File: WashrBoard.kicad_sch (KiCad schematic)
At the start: 37 parts, among them J1 TestPoint 5V, J10 ProgPoint GND, J2 USB_C_Receptacle_USB2.0_16P, J3 TestPoint GND, J4 TestPoint 3.3V, J5 JST XH, J6 ProgPoint 5V, J7 ProgPoint P9 GND, J8 ProgPointPoint D_P, J9 ProgPoint D_N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

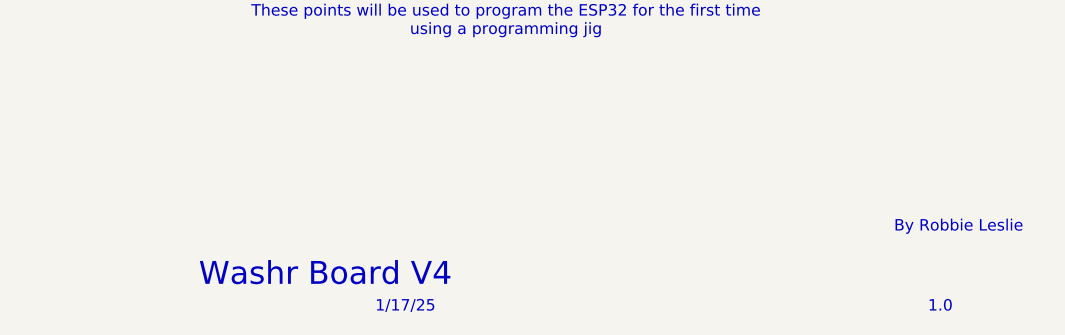
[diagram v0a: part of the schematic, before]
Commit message: Updated version, and moved old designs to archive repo
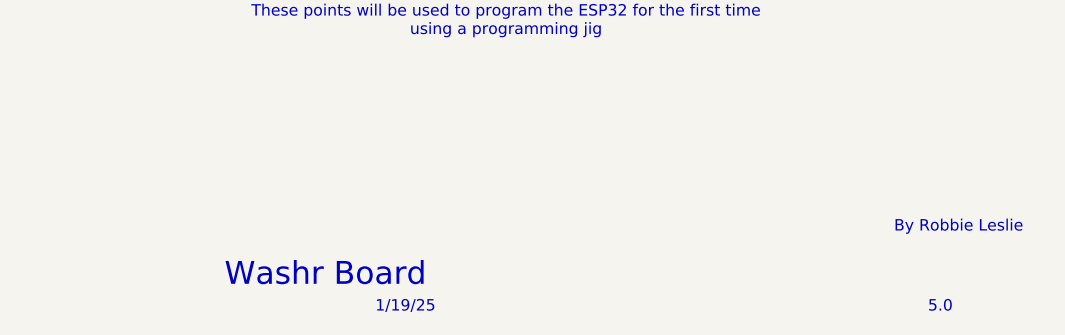
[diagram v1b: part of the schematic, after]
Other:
- note added: "1/19/25"
- note added: "5.0"
- note added: "Washr Board"
- note removed: "1.0"
- note removed: "1/17/25"
- note removed: "Washr Board V4"
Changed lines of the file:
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@@
 		)
 	)
-	(text "Washr Board V4"
+	(text "Washr Board"
 		(exclude_from_sim no)
 		(at 201.93 189.992 0)
@@
 		)
 	)
-	(text "1/17/25"
+	(text "1/19/25"
 		(exclude_from_sim no)
 		(at 210.82 193.548 0)
@@
 		)
 	)
-	(text "1.0"
+	(text "5.0"
 		(exclude_from_sim no)
 		(at 270.256 193.548 0)
@@
 	(label "SDA"
 		(at 54.61 92.71 0)
-		(fields_autoplaced yes)
 		(effects
 			(font
@@
 	(label "D_P"
 		(at 223.52 147.32 0)
-		(fields_autoplaced yes)
 		(effects
 			(font
@@
 	(label "D_P"
 		(at 63.5 151.13 0)
-		(fields_autoplaced yes)
 		(effects
 			(font
@@
 	(label "ProgGND"
 		(at 207.01 109.22 0)
-		(fields_autoplaced yes)
 		(effects
 			(font
@@
 	(label "D_P"
 		(at 92.71 34.29 0)
-		(fields_autoplaced yes)
 		(effects
 			(font
@@
 	(label "D_N"
 		(at 63.5 146.05 0)
-		(fields_autoplaced yes)
 		(effects
 			(font
@@
 	(label "ProgGND"
 		(at 223.52 135.89 0)
-		(fields_autoplaced yes)
 		(effects
 			(font
@@
 	(label "D-"
 		(at 213.36 81.28 0)
-		(fields_autoplaced yes)
 		(effects
 			(font
@@
 	(label "D+"
 		(at 213.36 83.82 0)
-		(fields_autoplaced yes)
 		(effects
 			(font
@@
 	(label "D_N"
 		(at 223.52 157.48 0)
-		(fields_autoplaced yes)
 		(effects
 			(font
@@
 	(label "D-"
 		(at 110.49 31.75 0)
-		(fields_autoplaced yes)
 		(effects
 			(font
@@
 	(label "SCL"
 		(at 54.61 90.17 0)
-		(fields_autoplaced yes)
 		(effects
 			(font
@@
 	(label "D_N"
 		(at 92.71 31.75 0)
-		(fields_autoplaced yes)
 		(effects
 			(font
@@
 	(label "SCL"
 		(at 177.8 66.04 0)
-		(fields_autoplaced yes)
 		(effects
 			(font
@@
 	(label "D+"
 		(at 110.49 34.29 0)
-		(fields_autoplaced yes)
 		(effects
 			(font
@@
 	(label "SDA"
 		(at 177.8 63.5 0)
-		(fields_autoplaced yes)
-		(effects
-			(font
+		(effects
+			(font

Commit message: Updated silkscreen
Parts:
- J1: TestValue (none) -> 5V
- J10: ProgPoint (none) -> PGND
- J3: TestValue (none) -> GND
- J4: TestValue (none) -> 3.3V
- J6: ProgPoint (none) -> 5V
- J7: ProgPoint (none) -> GND
- J8: ProgPoint (none) -> D_P
- J9: ProgPoint (none) -> D_N
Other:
- moved on the sheet: J1, J3, J4
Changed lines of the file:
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@@
 	(symbol
 		(lib_id "power:VBUS")
-		(at 26.67 60.96 90)
+		(at 129.54 157.48 270)
+		(mirror x)
 		(unit 1)
 		(exclude_from_sim no)
@@
 		(fields_autoplaced yes)
 		(property "Reference" "#PWR01"
-			(at 30.48 60.96 0)
+			(at 125.73 157.48 0)
 			(effects
 				(font
@@
 		)
 		(property "Value" "VBUS"
-			(at 22.86 60.9599 90)
+			(at 133.35 157.4799 90)
 			(effects
 				(font
@@
 		)
 		(property "Footprint" ""
-			(at 26.67 60.96 0)
+			(at 129.54 157.48 0)
 			(effects
 				(font
@@
 		)
 		(property "Datasheet" ""
-			(at 26.67 60.96 0)
+			(at 129.54 157.48 0)
 			(effects
 				(font
@@
 		)
 		(property "Description" "Power symbol creates a global label with name \"VBUS\""
-			(at 26.67 60.96 0)
+			(at 129.54 157.48 0)
 			(effects
 				(font
@@
 			)
 		)
+		(property "ProgPoint" "PGND"
+			(at 238.76 135.89 0)
+			(effects
+				(font
+					(size 1.27 1.27)
+				)
+				(hide yes)
+			)
+		)
 		(pin "1"
 		)
@@
 			)
 		)
+		(property "ProgPoint" "5V"
+			(at 218.44 125.73 0)
+			(effects
+				(font
+					(size 1.27 1.27)
+				)
+				(hide yes)
+			)
+		)
 		(pin "1"
 		)
@@
 			)
 		)
+		(property "ProgPoint" "D_P"
+			(at 218.44 147.32 0)
+			(effects
+				(font
+					(size 1.27 1.27)
+				)
+				(hide yes)
+			)
+		)
 		(pin "1"
 		)
@@
 			)
 		)
+		(property "ProgPoint" "D_N"
+			(at 218.44 157.48 0)
+			(effects
+				(font
+					(size 1.27 1.27)
+				)
+				(hide yes)
+			)
+		)
 		(pin "1"
 		)
@@
 	(symbol
 		(lib_id "Connector_Generic:Conn_01x01")
-		(at 48.26 71.12 180)
+		(at 124.46 168.91 180)
 		(unit 1)
 		(exclude_from_sim no)
@@
 		(fields_autoplaced yes)
 		(property "Reference" "J3"
-			(at 48.26 64.77 0)
+			(at 124.46 162.56 0)
 			(effects
 				(font
@@
 		)
 		(property "Value" "TestPoint GND"
-			(at 48.26 67.31 0)
+			(at 124.46 165.1 0)
 			(effects
 				(font
@@
 		)
 		(property "Footprint" "TestPoint:TestPoint_Pad_D1.0mm"
-			(at 48.26 71.12 0)
+			(at 124.46 168.91 0)
 			(effects
 				(font
@@
 		)
 		(property "Datasheet" "~"
-			(at 48.26 71.12 0)
+			(at 124.46 168.91 0)
 			(effects
 				(font
@@
 		)
 		(property "Description" "Generic connector, single row, 01x01, script generated (kicad-library-utils/schlib/autogen/connector/)"
-			(at 48.26 71.12 0)
+			(at 124.46 168.91 0)
 			(effects
 				(font
@@
 		)
 		(property "Manufacturer Part Number" ""
-			(at 48.26 71.12 0)
+			(at 124.46 168.91 0)
+			(effects
+				(font
+					(size 1.27 1.27)
+				)
+				(hide yes)
+			)
+		)
+		(property "TestValue" "GND"
+			(at 124.46 168.91 0)
 			(effects
 				(font
@@
 	(symbol
 		(lib_id "power:GND")
-		(at 53.34 71.12 90)
+		(at 129.54 168.91 90)
 		(unit 1)
 		(exclude_from_sim no)
@@
 		(fields_autoplaced yes)
 		(property "Reference" "#PWR07"
-			(at 59.69 71.12 0)
+			(at 135.89 168.91 0)
 			(effects
 				(font
@@
 		)
 		(property "Value" "GND"
-			(at 57.15 71.1199 90)
+			(at 133.35 168.9099 90)
 			(effects
 				(font
@@
 		)
 		(property "Footprint" ""
-			(at 53.34 71.12 0)
+			(at 129.54 168.91 0)
 			(effects
 				(font
@@
 		)
 		(property "Datasheet" ""
-			(at 53.34 71.12 0)
+			(at 129.54 168.91 0)
 			(effects
 				(font
@@
 		)
 		(property "Description" "Power symbol creates a global label with name \"GND\" , ground"
-			(at 53.34 71.12 0)
+			(at 129.54 168.91 0)
 			(effects
 				(font
@@
 	(symbol
 		(lib_id "Connector_Generic:Conn_01x01")
-		(at 31.75 60.96 0)
+		(at 124.46 157.48 0)
+		(mirror y)
 		(unit 1)
 		(exclude_from_sim no)
@@
 		(fields_autoplaced yes)
 		(property "Reference" "J1"
-			(at 34.29 59.6899 0)
+			(at 121.92 156.2099 0)
 			(effects
 				(font
@@
 		)
 		(property "Value" "TestPoint 5V"
-			(at 34.29 62.2299 0)
+			(at 121.92 158.7499 0)
 			(effects
 				(font
@@
 		)
 		(property "Footprint" "TestPoint:TestPoint_Pad_D1.0mm"
-			(at 31.75 60.96 0)
+			(at 124.46 157.48 0)
 			(effects
 				(font
@@
 		)
 		(property "Datasheet" "~"
-			(at 31.75 60.96 0)
+			(at 124.46 157.48 0)
 			(effects
 				(font
@@
 		)
 		(property "Description" "Generic connector, single row, 01x01, script generated (kicad-library-utils/schlib/autogen/connector/)"
-			(at 31.75 60.96 0)
+			(at 124.46 157.48 0)
 			(effects
 				(font
@@
 		)
 		(property "Manufacturer Part Number" ""
-			(at 31.75 60.96 0)
+			(at 124.46 157.48 0)
+			(effects
+				(font
+					(size 1.27 1.27)
+				)
+				(hide yes)
+			)
+		)
+		(property "TestValue" "5V"
+			(at 124.46 157.48 0)
 			(effects
 				(font
@@
 			)
 		)
+		(property "ProgPoint" "GND"
+			(at 218.44 135.89 0)
+			(effects
+				(font
+					(size 1.27 1.27)
+				)
+				(hide yes)
+			)
+		)
 		(pin "1"
 		)
@@
 	(symbol
 		(lib_id "Connector_Generic:Conn_01x01")
-		(at 59.69 60.96 180)
+		(at 124.46 180.34 180)
 		(unit 1)
 		(exclude_from_sim no)
@@
 		(fields_autoplaced yes)
 		(property "Reference" "J4"
-			(at 59.69 54.61 0)
+			(at 124.46 173.99 0)
 			(effects
 				(font
@@
 		)
 		(property "Value" "TestPoint 3.3V"
-			(at 59.69 57.15 0)
+			(at 124.46 176.53 0)
 			(effects
 				(font
@@
 		)
 		(property "Footprint" "TestPoint:TestPoint_Pad_D1.0mm"
-			(at 59.69 60.96 0)
+			(at 124.46 180.34 0)
 			(effects
 				(font
@@
 		)
 		(property "Datasheet" "~"
-			(at 59.69 60.96 0)
+			(at 124.46 180.34 0)
 			(effects
 				(font
@@
 		)
 		(property "Description" "Generic connector, single row, 01x01, script generated (kicad-library-utils/schlib/autogen/connector/)"
-			(at 59.69 60.96 0)
+			(at 124.46 180.34 0)
 			(effects
 				(font
@@
 		)
 		(property "Manufacturer Part Number" ""
-			(at 59.69 60.96 0)
+			(at 124.46 180.34 0)
+			(effects
+				(font
+					(size 1.27 1.27)
+				)
+				(hide yes)
+			)
+		)
+		(property "TestValue" "3.3V"
+			(at 124.46 180.34 0)
 			(effects
 				(font
@@
 	(symbol
 		(lib_id "power:+3.3V")
-		(at 64.77 60.96 270)
+		(at 129.54 180.34 270)
 		(unit 1)
 		(exclude_from_sim no)
@@
 		(fields_autoplaced yes)
 		(property "Reference" "#PWR010"
-			(at 60.96 60.96 0)
+			(at 125.73 180.34 0)
 			(effects
 				(font
@@
 		)
 		(property "Value" "+3.3V"
-			(at 68.58 60.9599 90)
+			(at 133.35 180.3399 90)
 			(effects
 				(font
@@
 		)
 		(property "Footprint" ""
-			(at 64.77 60.96 0)
+			(at 129.54 180.34 0)
 			(effects
 				(font
@@
 		)
 		(property "Datasheet" ""
-			(at 64.77 60.96 0)
+			(at 129.54 180.34 0)
 			(effects
 				(font
@@
 		)
 		(property "Description" "Power symbol creates a global label with name \"+3.3V\""
-			(at 64.77 60.96 0)
+			(at 129.54 180.34 0)
 			(effects
 				(font

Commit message: Annotated schematic
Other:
- note added: "5V to 3.3V Regulator"
- note added: "ESP32 C3"
- note added: "IMU"
- note added: "JST Power Connector"
- note added: "Mounting Holes"
- note added: "P9 Button"
- note added: "Programming Points"
- note added: "Test Points"
- note added: "USB Port"
- note added: "USB Protection"
- moved on the sheet: U2
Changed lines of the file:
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@@
 	(wire
 		(pts
-			(xy 92.71 31.75) (xy 96.52 31.75)
+			(xy 96.52 36.83) (xy 100.33 36.83)
 		)
 		(stroke
@@
 	(wire
 		(pts
-			(xy 92.71 34.29) (xy 96.52 34.29)
+			(xy 96.52 39.37) (xy 100.33 39.37)
 		)
 		(stroke
@@
 	(wire
 		(pts
-			(xy 106.68 31.75) (xy 110.49 31.75)
+			(xy 110.49 36.83) (xy 114.3 36.83)
 		)
 		(stroke
@@
 	(wire
 		(pts
-			(xy 106.68 34.29) (xy 110.49 34.29)
+			(xy 110.49 39.37) (xy 114.3 39.37)
 		)
 		(stroke
@@
 		)
 	)
+	(text "IMU"
+		(exclude_from_sim no)
+		(at 77.47 69.088 0)
+		(effects
+			(font
+				(size 2.54 2.54)
+			)
+		)
+	)
+	(text "5V to 3.3V Regulator"
+		(exclude_from_sim no)
+		(at 46.482 18.542 0)
+		(effects
+			(font
+				(size 2.54 2.54)
+			)
+		)
+	)
+	(text "Test Points"
+		(exclude_from_sim no)
+		(at 125.222 152.654 0)
+		(effects
+			(font
+				(size 1.905 1.905)
+			)
+		)
+	)
 	(text "Washr Board"
 		(exclude_from_sim no)
@@
 		)
 	)
+	(text "Programming Points"
+		(exclude_from_sim no)
+		(at 191.516 149.606 0)
+		(effects
+			(font
+				(size 2.54 2.54)
+			)
+		)
+	)
+	(text "JST Power Connector"
+		(exclude_from_sim no)
+		(at 122.936 111.252 0)
+		(effects
+			(font
+				(size 1.905 1.905)
+			)
+		)
+	)
 	(text "1/19/25"
 		(exclude_from_sim no)
@@
 	(text "JST Connector can be used as a locking alternantive to USB-C to provide power. Does not provide data."
 		(exclude_from_sim no)
-		(at 143.51 123.19 0)
+		(at 131.318 122.428 0)
 		(effects
 			(font
@@
 		)
 	)
+	(text "ESP32 C3"
+		(exclude_from_sim no)
+		(at 236.474 23.114 0)
+		(effects
+			(font
+				(size 2.54 2.54)
+			)
+		)
+	)
+	(text "USB Port"
+		(exclude_from_sim no)
+		(at 40.132 119.888 0)
+		(effects
+			(font
+				(size 2.54 2.54)
+			)
+		)
+	)
 	(text "By Robbie Leslie"
 		(exclude_from_sim no)
-		(at 272.288 184.658 0)
+		(at 272.034 189.738 0)
 		(effects
 			(font
-				(size 1.27 1.27)
+				(size 1.905 1.905)
+			)
+		)
+	)
+	(text "USB Protection"
+		(exclude_from_sim no)
+		(at 106.68 21.082 0)
+		(effects
+			(font
+				(size 2.54 2.54)
 			)
 		)
@@
 		)
 	)
+	(text "P9 Button"
+		(exclude_from_sim no)
+		(at 234.442 116.586 0)
+		(effects
+			(font
+				(size 1.27 1.27)
+			)
+		)
+	)
 	(text "5.0"
 		(exclude_from_sim no)
@@
 		)
 	)
+	(text "Mounting Holes"
+		(exclude_from_sim no)
+		(at 63.246 186.944 0)
+		(effects
+			(font
+				(size 1.905 1.905)
+			)
+		)
+	)
 	(label "SDA"
 		(at 54.61 92.71 0)
@@
 	)
 	(label "D_P"
-		(at 92.71 34.29 0)
+		(at 96.52 39.37 0)
 		(effects
 			(font
@@
 	)
 	(label "D-"
-		(at 110.49 31.75 0)
+		(at 114.3 36.83 0)
 		(effects
 			(font
@@
 	)
 	(label "D_N"
-		(at 92.71 31.75 0)
+		(at 96.52 36.83 0)
 		(effects
 			(font
@@
 	)
 	(label "D+"
-		(at 110.49 34.29 0)
+		(at 114.3 39.37 0)
 		(effects
 			(font
@@
 	(symbol
 		(lib_id "power:VBUS")
-		(at 101.6 26.67 0)
+		(at 105.41 31.75 0)
 		(unit 1)
 		(exclude_from_sim no)
@@
 		(fields_autoplaced yes)
 		(property "Reference" "#PWR016"
-			(at 101.6 30.48 0)
+			(at 105.41 35.56 0)
 			(effects
 				(font
@@
 		)
 		(property "Value" "VBUS"
-			(at 101.6 21.59 0)
+			(at 105.41 26.67 0)
 			(effects
 				(font
@@
 		)
 		(property "Footprint" ""
-			(at 101.6 26.67 0)
+			(at 105.41 31.75 0)
 			(effects
 				(font
@@
 		)
 		(property "Datasheet" ""
-			(at 101.6 26.67 0)
+			(at 105.41 31.75 0)
 			(effects
 				(font
@@
 		)
 		(property "Description" "Power symbol creates a global label with name \"VBUS\""
-			(at 101.6 26.67 0)
+			(at 105.41 31.75 0)
 			(effects
 				(font
@@
 	(symbol
 		(lib_id "Power_Protection:USBLC6-2SC6")
-		(at 101.6 31.75 0)
+		(at 105.41 36.83 0)
 		(unit 1)
 		(exclude_from_sim no)
@@
 		(fields_autoplaced yes)
 		(property "Reference" "U2"
-			(at 103.2511 24.13 0)
+			(at 107.0611 29.21 0)
 			(effects
 				(font
@@
 		)
 		(property "Value" "USBLC6-2SC6"
-			(at 103.2511 26.67 0)
+			(at 107.0611 31.75 0)
 			(effects
 				(font
@@
 		)
 		(property "Footprint" "Package_TO_SOT_SMD:SOT-23-6"
-			(at 102.87 38.1 0)
+			(at 106.68 43.18 0)
 			(effects
 				(font
@@
 		)
 		(property "Datasheet" "https://www.st.com/resource/en/datasheet/usblc6-2.pdf"
-			(at 102.87 40.005 0)
+			(at 106.68 45.085 0)
 			(effects
 				(font
@@
 		)
 		(property "Description" "Very low capacitance ESD protection diode, 2 data-line, SOT-23-6"
-			(at 101.6 31.75 0)
+			(at 105.41 36.83 0)
 			(effects
 				(font
@@
 		)
 		(property "Manufacturer Part Number" "USBLC6-2SC6"
-			(at 101.6 31.75 0)
+			(at 105.41 36.83 0)
 			(effects
 				(font
@@
 	(symbol
 		(lib_id "power:GND")
-		(at 101.6 39.37 0)
+		(at 105.41 44.45 0)
 		(unit 1)
 		(exclude_from_sim no)
@@
 		(fields_autoplaced yes)
 		(property "Reference" "#PWR017"
-			(at 101.6 45.72 0)
+			(at 105.41 50.8 0)
 			(effects
 				(font
@@
 		)
 		(property "Value" "GND"
-			(at 101.6 44.45 0)
+			(at 105.41 49.53 0)
 			(effects
 				(font
@@
 		)
 		(property "Footprint" ""
-			(at 101.6 39.37 0)
+			(at 105.41 44.45 0)
 			(effects
 				(font
@@
 		)
 		(property "Datasheet" ""
-			(at 101.6 39.37 0)
+			(at 105.41 44.45 0)
 			(effects
 				(font
@@
 		)
 		(property "Description" "Power symbol creates a global label with name \"GND\" , ground"
-			(at 101.6 39.37 0)
+			(at 105.41 44.45 0)
 			(effects
 				(font

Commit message: Swapped JST XH for GH connector
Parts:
- J5: value JST XH -> JST GH; footprint Connector_JST:JST_XH_S2B-XH-A-1_1x02_P2.50mm_Horizontal -> Connector_JST:JST_GH_SM02B-GHS-TB_1x02-1MP_P1.25mm_Horizontal; Manufacturer Part Number S2B-XH-A-1 -> SM02B-GHS-TB
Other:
- note added: "1/26/25"
- note added: "5.1"
- note removed: "1/19/25"
- note removed: "5.0"
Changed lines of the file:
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@@
 		)
 	)
-	(text "1/19/25"
+	(text "1/26/25"
 		(exclude_from_sim no)
 		(at 210.82 193.548 0)
@@
 		)
 	)
-	(text "5.0"
+	(text "5.1"
 		(exclude_from_sim no)
 		(at 270.256 193.548 0)
@@
 			)
 		)
-		(property "Value" "JST XH"
+		(property "Value" "JST GH"
 			(at 125.73 118.1099 0)
 			(effects
@@
 			)
 		)
-		(property "Footprint" "Connector_JST:JST_XH_S2B-XH-A-1_1x02_P2.50mm_Horizontal"
+		(property "Footprint" "Connector_JST:JST_GH_SM02B-GHS-TB_1x02-1MP_P1.25mm_Horizontal"
 			(at 123.19 115.57 0)
 			(effects
@@
 			)
 		)
-		(property "Manufacturer Part Number" "S2B-XH-A-1"
+		(property "Manufacturer Part Number" "SM02B-GHS-TB"
 			(at 123.19 115.57 0)
 			(effects

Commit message: Swapped screwholes to ISO 7380
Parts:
- H1, H2, H3, H4: footprint MountingHole:MountingHole_3.2mm_M3_DIN965_Pad -> MountingHole:MountingHole_3.2mm_M3_ISO7380_Pad
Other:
- note added: "2/1/25"
- note added: "5.2"
- note removed: "1/26/25"
- note removed: "5.1"
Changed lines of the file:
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@@
 		)
 	)
-	(text "1/26/25"
+	(text "2/1/25"
 		(exclude_from_sim no)
 		(at 210.82 193.548 0)
@@
 		)
 	)
-	(text "5.1"
+	(text "5.2"
 		(exclude_from_sim no)
 		(at 270.256 193.548 0)
@@
 			)
 		)
-		(property "Footprint" "MountingHole:MountingHole_3.2mm_M3_DIN965_Pad"
+		(property "Footprint" "MountingHole:MountingHole_3.2mm_M3_ISO7380_Pad"
 			(at 40.64 191.77 0)
 			(effects
@@
 			)
 		)
-		(property "Footprint" "MountingHole:MountingHole_3.2mm_M3_DIN965_Pad"
+		(property "Footprint" "MountingHole:MountingHole_3.2mm_M3_ISO7380_Pad"
 			(at 19.05 180.34 0)
 			(effects
@@
 			)
 		)
-		(property "Footprint" "MountingHole:MountingHole_3.2mm_M3_DIN965_Pad"
+		(property "Footprint" "MountingHole:MountingHole_3.2mm_M3_ISO7380_Pad"
 			(at 40.64 180.34 0)
 			(effects
@@
 			)
 		)
-		(property "Footprint" "MountingHole:MountingHole_3.2mm_M3_DIN965_Pad"
+		(property "Footprint" "MountingHole:MountingHole_3.2mm_M3_ISO7380_Pad"
 			(at 19.05 190.5 0)
 			(effects
